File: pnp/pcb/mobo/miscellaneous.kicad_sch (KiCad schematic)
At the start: 7 parts

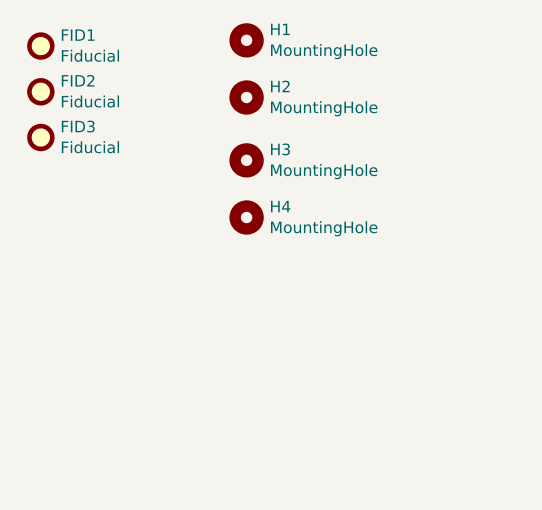
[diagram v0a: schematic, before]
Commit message: Connect all sub-sheets together
Refactored schematic is checked against existing lay-out.
Connectivity has stayed the same.
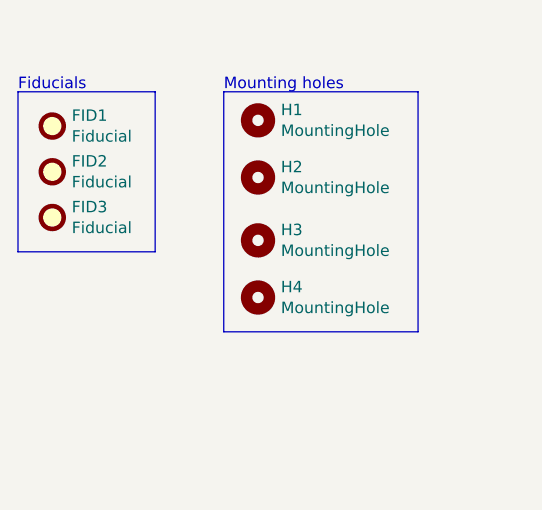
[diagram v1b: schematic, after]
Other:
- note added: "Fiducials"
- note added: "Mounting holes"
- moved on the sheet: FID1, FID2, FID3, H1, H2, H3, H4
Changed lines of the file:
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@@
 (kicad_sch (version 20211123) (generator eeschema)
   (paper "A4")
-  (symbol (lib_id "Mechanical:Fiducial") (at 133.35 87.63 0) (unit 1)
+  (polyline (pts (xy 175.26 119.38) (xy 153.67 119.38))
+    (stroke (width 0) (type default) (color 0 0 0 0))
+  )
+  (polyline (pts (xy 130.81 92.71) (xy 146.05 92.71))
+    (stroke (width 0) (type default) (color 0 0 0 0))
+  )
+  (polyline (pts (xy 146.05 92.71) (xy 146.05 110.49))
+    (stroke (width 0) (type default) (color 0 0 0 0))
+  )
+  (polyline (pts (xy 175.26 92.71) (xy 175.26 119.38))
+    (stroke (width 0) (type default) (color 0 0 0 0))
+  )
+  (polyline (pts (xy 153.67 92.71) (xy 153.67 119.38))
+    (stroke (width 0) (type default) (color 0 0 0 0))
+  )
+  (polyline (pts (xy 130.81 92.71) (xy 130.81 110.49))
+    (stroke (width 0) (type default) (color 0 0 0 0))
+  )
+  (polyline (pts (xy 146.05 110.49) (xy 130.81 110.49))
+    (stroke (width 0) (type default) (color 0 0 0 0))
+  )
+  (polyline (pts (xy 153.67 92.71) (xy 175.26 92.71))
+    (stroke (width 0) (type default) (color 0 0 0 0))
+  )
+  (text "Fiducials" (at 130.81 92.71 0)
+    (effects (font (size 1.27 1.27)) (justify left bottom))
+  )
+  (text "Mounting holes" (at 153.67 92.71 0)
+    (effects (font (size 1.27 1.27)) (justify left bottom))
+  )
+  (symbol (lib_id "Mechanical:Fiducial") (at 134.62 96.52 0) (unit 1)
     (in_bom yes) (on_board yes)
-    (property "Reference" "FID1" (id 0) (at 135.509 86.4616 0)
+    (property "Reference" "FID1" (id 0) (at 136.779 95.3516 0)
       (effects (font (size 1.27 1.27)) (justify left))
     )
-    (property "Value" "Fiducial" (id 1) (at 135.509 88.773 0)
+    (property "Value" "Fiducial" (id 1) (at 136.779 97.663 0)
       (effects (font (size 1.27 1.27)) (justify left))
     )
-    (property "Footprint" "Fiducial:Fiducial_1mm_Mask2mm" (id 2) (at 133.35 87.63 0)
+    (property "Footprint" "Fiducial:Fiducial_1mm_Mask2mm" (id 2) (at 134.62 96.52 0)
       (effects (font (size 1.27 1.27)) hide)
     )
-    (property "Datasheet" "" (id 3) (at 133.35 87.63 0)
+    (property "Datasheet" "" (id 3) (at 134.62 96.52 0)
       (effects (font (size 1.27 1.27)) hide)
     )
   )
-  (symbol (lib_id "Mechanical:Fiducial") (at 133.35 97.79 0) (unit 1)
+  (symbol (lib_id "Mechanical:Fiducial") (at 134.62 106.68 0) (unit 1)
     (in_bom yes) (on_board yes)
-    (property "Reference" "FID3" (id 0) (at 135.509 96.6216 0)
+    (property "Reference" "FID3" (id 0) (at 136.779 105.5116 0)
       (effects (font (size 1.27 1.27)) (justify left))
     )
-    (property "Value" "Fiducial" (id 1) (at 135.509 98.933 0)
+    (property "Value" "Fiducial" (id 1) (at 136.779 107.823 0)
       (effects (font (size 1.27 1.27)) (justify left))
     )
-    (property "Footprint" "Fiducial:Fiducial_1mm_Mask2mm" (id 2) (at 133.35 97.79 0)
+    (property "Footprint" "Fiducial:Fiducial_1mm_Mask2mm" (id 2) (at 134.62 106.68 0)
       (effects (font (size 1.27 1.27)) hide)
     )
-    (property "Datasheet" "" (id 3) (at 133.35 97.79 0)
+    (property "Datasheet" "" (id 3) (at 134.62 106.68 0)
       (effects (font (size 1.27 1.27)) hide)
     )
   )
-  (symbol (lib_id "Mechanical:MountingHole") (at 156.21 100.33 0) (unit 1)
+  (symbol (lib_id "Mechanical:MountingHole") (at 157.48 109.22 0) (unit 1)
     (in_bom yes) (on_board yes)
-    (property "Reference" "H3" (id 0) (at 158.75 99.1616 0)
+    (property "Reference" "H3" (id 0) (at 160.02 108.0516 0)
       (effects (font (size 1.27 1.27)) (justify left))
     )
-    (property "Value" "MountingHole" (id 1) (at 158.75 101.473 0)
+    (property "Value" "MountingHole" (id 1) (at 160.02 110.363 0)
       (effects (font (size 1.27 1.27)) (justify left))
     )
-    (property "Footprint" "MountingHole:MountingHole_3.2mm_M3_DIN965_Pad" (id 2) (at 156.21 100.33 0)
+    (property "Footprint" "MountingHole:MountingHole_3.2mm_M3_DIN965_Pad" (id 2) (at 157.48 109.22 0)
       (effects (font (size 1.27 1.27)) hide)
     )
-    (property "Datasheet" "" (id 3) (at 156.21 100.33 0)
+    (property "Datasheet" "" (id 3) (at 157.48 109.22 0)
       (effects (font (size 1.27 1.27)) hide)
     )
   )
-  (symbol (lib_id "Mechanical:Fiducial") (at 133.35 92.71 0) (unit 1)
+  (symbol (lib_id "Mechanical:Fiducial") (at 134.62 101.6 0) (unit 1)
     (in_bom yes) (on_board yes)
-    (property "Reference" "FID2" (id 0) (at 135.509 91.5416 0)
+    (property "Reference" "FID2" (id 0) (at 136.779 100.4316 0)
       (effects (font (size 1.27 1.27)) (justify left))
     )
-    (property "Value" "Fiducial" (id 1) (at 135.509 93.853 0)
+    (property "Value" "Fiducial" (id 1) (at 136.779 102.743 0)
       (effects (font (size 1.27 1.27)) (justify left))
     )
-    (property "Footprint" "Fiducial:Fiducial_1mm_Mask2mm" (id 2) (at 133.35 92.71 0)
+    (property "Footprint" "Fiducial:Fiducial_1mm_Mask2mm" (id 2) (at 134.62 101.6 0)
       (effects (font (size 1.27 1.27)) hide)
     )
-    (property "Datasheet" "" (id 3) (at 133.35 92.71 0)
+    (property "Datasheet" "" (id 3) (at 134.62 101.6 0)
       (effects (font (size 1.27 1.27)) hide)
     )
   )
-  (symbol (lib_id "Mechanical:MountingHole") (at 156.21 106.68 0) (unit 1)
+  (symbol (lib_id "Mechanical:MountingHole") (at 157.48 115.57 0) (unit 1)
     (in_bom yes) (on_board yes)
-    (property "Reference" "H4" (id 0) (at 158.75 105.5116 0)
+    (property "Reference" "H4" (id 0) (at 160.02 114.4016 0)
       (effects (font (size 1.27 1.27)) (justify left))
     )
-    (property "Value" "MountingHole" (id 1) (at 158.75 107.823 0)
+    (property "Value" "MountingHole" (id 1) (at 160.02 116.713 0)
       (effects (font (size 1.27 1.27)) (justify left))
     )
-    (property "Footprint" "MountingHole:MountingHole_3.2mm_M3_DIN965_Pad" (id 2) (at 156.21 106.68 0)
+    (property "Footprint" "MountingHole:MountingHole_3.2mm_M3_DIN965_Pad" (id 2) (at 157.48 115.57 0)
       (effects (font (size 1.27 1.27)) hide)
     )
-    (property "Datasheet" "" (id 3) (at 156.21 106.68 0)
+    (property "Datasheet" "" (id 3) (at 157.48 115.57 0)
       (effects (font (size 1.27 1.27)) hide)
     )
   )
-  (symbol (lib_id "Mechanical:MountingHole") (at 156.21 86.995 0) (unit 1)
+  (symbol (lib_id "Mechanical:MountingHole") (at 157.48 95.885 0) (unit 1)
     (in_bom yes) (on_board yes)
-    (property "Reference" "H1" (id 0) (at 158.75 85.8266 0)
+    (property "Reference" "H1" (id 0) (at 160.02 94.7166 0)
       (effects (font (size 1.27 1.27)) (justify left))
     )
-    (property "Value" "MountingHole" (id 1) (at 158.75 88.138 0)
+    (property "Value" "MountingHole" (id 1) (at 160.02 97.028 0)
       (effects (font (size 1.27 1.27)) (justify left))
     )
-    (property "Footprint" "MountingHole:MountingHole_3.2mm_M3_DIN965_Pad" (id 2) (at 156.21 86.995 0)
+    (property "Footprint" "MountingHole:MountingHole_3.2mm_M3_DIN965_Pad" (id 2) (at 157.48 95.885 0)
       (effects (font (size 1.27 1.27)) hide)
     )
-    (property "Datasheet" "" (id 3) (at 156.21 86.995 0)
+    (property "Datasheet" "" (id 3) (at 157.48 95.885 0)
       (effects (font (size 1.27 1.27)) hide)
     )
   )
-  (symbol (lib_id "Mechanical:MountingHole") (at 156.21 93.345 0) (unit 1)
+  (symbol (lib_id "Mechanical:MountingHole") (at 157.48 102.235 0) (unit 1)
     (in_bom yes) (on_board yes)
-    (property "Reference" "H2" (id 0) (at 158.75 92.1766 0)
+    (property "Reference" "H2" (id 0) (at 160.02 101.0666 0)
       (effects (font (size 1.27 1.27)) (justify left))
     )
-    (property "Value" "MountingHole" (id 1) (at 158.75 94.488 0)
+    (property "Value" "MountingHole" (id 1) (at 160.02 103.378 0)
       (effects (font (size 1.27 1.27)) (justify left))
     )
-    (property "Footprint" "MountingHole:MountingHole_3.2mm_M3_DIN965_Pad" (id 2) (at 156.21 93.345 0)
+    (property "Footprint" "MountingHole:MountingHole_3.2mm_M3_DIN965_Pad" (id 2) (at 157.48 102.235 0)
       (effects (font (size 1.27 1.27)) hide)
     )
-    (property "Datasheet" "" (id 3) (at 156.21 93.345 0)
+    (property "Datasheet" "" (id 3) (at 157.48 102.235 0)
       (effects (font (size 1.27 1.27)) hide)
     )

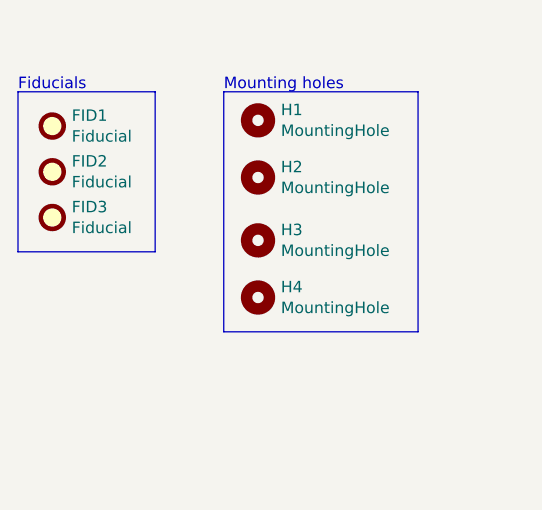
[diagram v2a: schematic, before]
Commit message: moving mobo-rev04b0 into mobo-rev04 branch from old repo
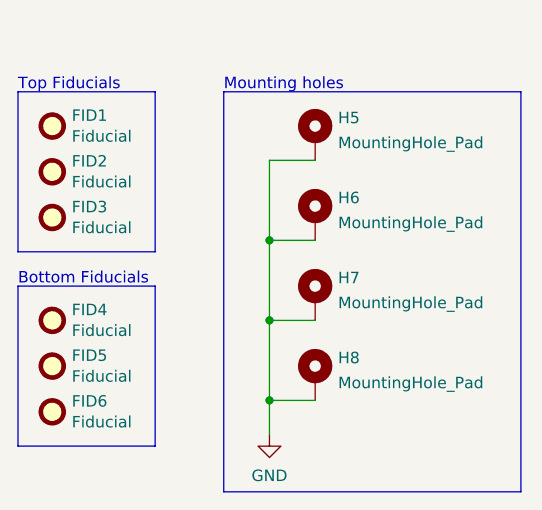
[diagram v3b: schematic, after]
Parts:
- removed H1, H2, H3, H4: MountingHole, MountingHole:MountingHole_3.2mm_M3_DIN965_Pad, symbol Mechanical:MountingHole
- added FID4, FID5, FID6: Fiducial, Fiducial:Fiducial_1mm_Mask2mm, symbol Mechanical:Fiducial
- added H5, H6, H7, H8: MountingHole_Pad, MountingHole:MountingHole_3.2mm_M3_DIN965_Pad, symbol Mechanical:MountingHole_Pad
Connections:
- new net GND: H5.1, H6.1, H7.1, H8.1
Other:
- note added: "Bottom Fiducials"
- note added: "Top Fiducials"
- note removed: "Fiducials"
- company: (none) -> Opulo
- title: (none) -> LumenPnP Motherboard
